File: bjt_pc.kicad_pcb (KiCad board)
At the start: 2 copper layers, 130 x 79 mm, 72 parts, among them J1 Conn_02x10_Odd_Even

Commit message: Finalized compressed 1.0
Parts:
- Qand11, Qand12, Qand13, Qand21, Qand22, Qand23, Qbuf1, Qbuf2, Qmux1, Qmux2, Qmux3, Qmux4, Qmux5, Qmux6, Qsrl1, Qsrl2, Qsrl3, Qtsb2, Qtsb3, Qtsb4, Qtsb5, Qtsb6: footprint Custom_Footprints:TO-92_Inline_disp -> Package_TO_SOT_THT:TO-92_Inline_Wide
- Qtsb1: footprint Custom_Footprints:TO-92_Inline_PNP_disp -> Package_TO_SOT_THT:TO-92_Inline_Wide
- moved R1 57.2 mm to (143.5, 105.4), turned to 90 degrees
- moved REF** 50.6 mm to (167.6, 85.0)
- moved G*** 49.4 mm to (144.0, 114.0)
- moved R4 48.9 mm to (147.3, 97.8), turned to -90 degrees
- moved Qtsb4 46.2 mm to (138.4, 94.0), turned to 0 degrees
- moved sDATA4 43.9 mm to (139.7, 105.4), turned to 90 degrees
- moved sDATA1 43.0 mm to (132.1, 92.7), turned to -90 degrees
- moved R5 42.7 mm to (154.9, 105.4), turned to 90 degrees
- moved Qmux4 40.4 mm to (130.8, 104.1), turned to 180 degrees
- moved D1 37.4 mm to (177.8, 138.4), turned to 90 degrees
- moved Qtsb2 37.0 mm to (153.7, 109.2), turned to 0 degrees
- moved C1 35.3 mm to (174.0, 88.9), turned to 90 degrees
- moved Qtsb3 34.7 mm to (146.1, 94.0), turned to 0 degrees
- moved R33 32.3 mm to (109.2, 92.7)
- moved Qmux3 32.0 mm to (123.2, 104.1), turned to 180 degrees
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- renumbered DATA to D1
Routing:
- net /DATA: track 142.5 -> 65.2 mm
- net /WE: track 105.9 -> 67.8 mm, vias 0 -> 1
- net Net-(Qsrl2-B): track 54.0 -> 16.5 mm
- net /BUSo: track 64.1 -> 28.2 mm
- net /CLK: track 107.3 -> 72.0 mm, vias 1 -> 0
- net /nOE: track 17.6 -> 38.8 mm
- net /VCC: track 326.0 -> 306.7 mm
- net /AlwaysOn: track 25.5 -> 8.67 mm
- net /BUSi: track 77.9 -> 61.2 mm, vias 0 -> 1
- net Net-(Qtsb3-C): track 34.6 -> 18.4 mm
- net /RAW: track 35.0 -> 21.1 mm
- net Net-(Qtsb5-C): track 21.0 -> 7.62 mm
- net /OE: track 16.8 -> 30.1 mm
- net /LED: track 9.65 -> 22.7 mm
- net Net-(Qmux3-C): track 37.5 -> 25.3 mm
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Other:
- board size 130 x 79 mm -> 92 x 60 mm
- board text removed: "AND2"
- board text removed: "Buffer"
- board text removed: "MUX"
- board text removed: "SR Latch"
- board text removed: "TriStateBuffer"

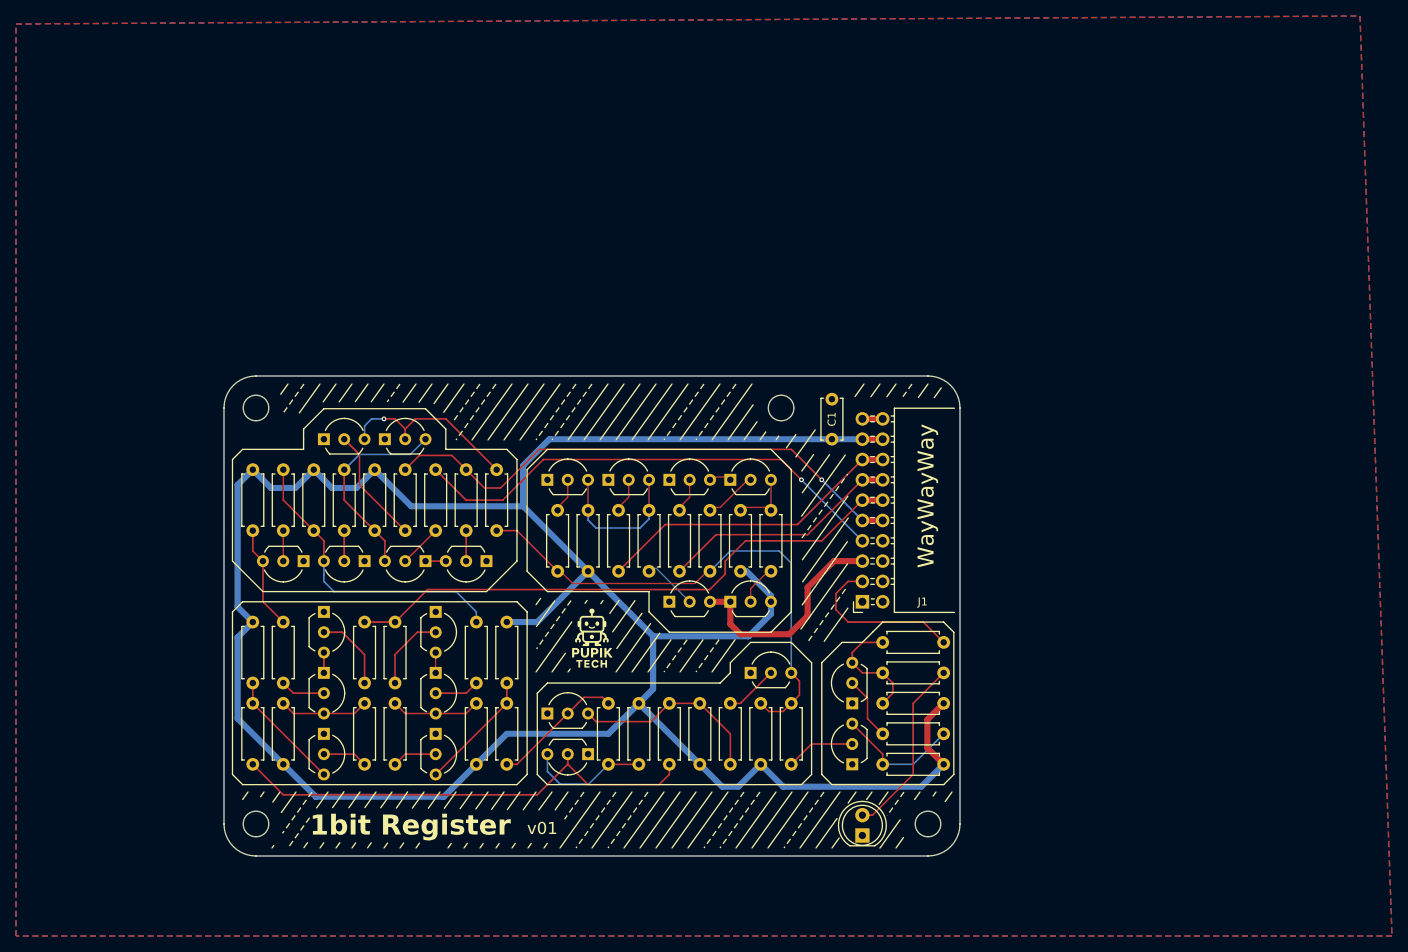
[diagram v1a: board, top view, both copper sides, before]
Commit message: Added Test Points
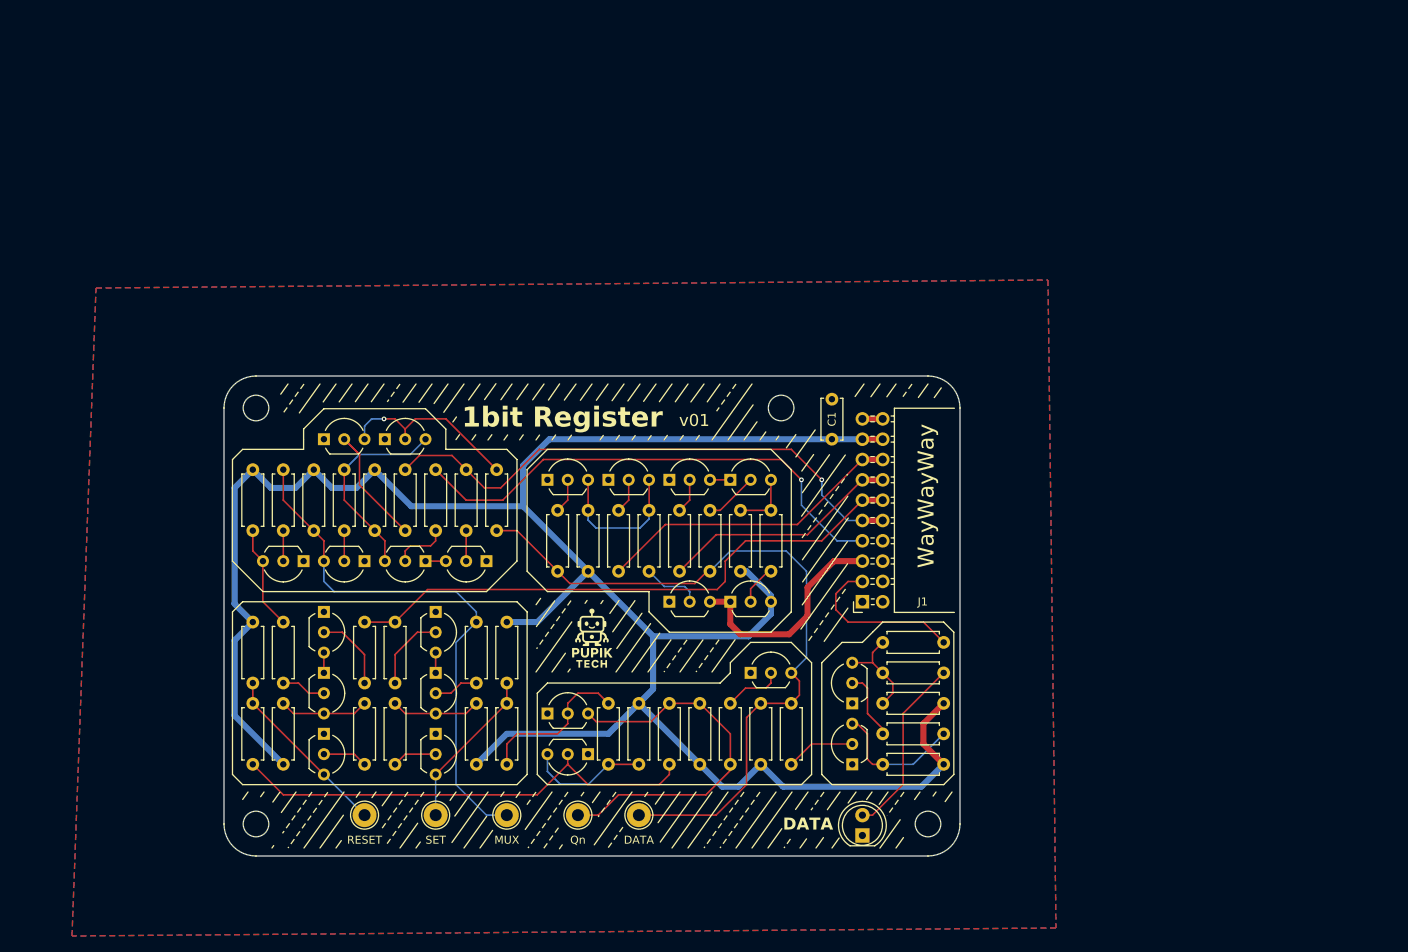
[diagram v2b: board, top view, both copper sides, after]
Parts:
- added DATA: TestPoint, TestPoint:TestPoint_THTPad_D3.0mm_Drill1.5mm, F.Cu at (149.9, 135.9)
- added MUX: TestPoint, TestPoint:TestPoint_THTPad_D3.0mm_Drill1.5mm, F.Cu at (133.3, 135.9)
- added Qn: TestPoint, TestPoint:TestPoint_THTPad_D3.0mm_Drill1.5mm, F.Cu at (142.2, 135.9)
- added RESET: TestPoint, TestPoint:TestPoint_THTPad_D3.0mm_Drill1.5mm, F.Cu at (115.6, 135.9)
- added SET: TestPoint, TestPoint:TestPoint_THTPad_D3.0mm_Drill1.5mm, F.Cu at (124.5, 135.9)
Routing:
- net Net-(Qmux2-C): track 38.0 -> 67.3 mm
- net /DATA: track 65.2 -> 92.2 mm
- net /VCC: track 306.7 -> 280.3 mm
- net Net-(Qsrl2-C): track 24.5 -> 46.7 mm
- net /R: track 15.1 -> 22.3 mm
- net /S: track 15.1 -> 20.2 mm
- net Net-(Qsrl2-B): track 16.5 -> 19.9 mm
- net Net-(Qbuf1-C): track 14.8 -> 12.3 mm
- net /BUSi: track 61.2 -> 63.1 mm
- net Net-(Qmux3-B): track 5.39 -> 6.88 mm
- net Net-(Qbuf2-C): track 15.9 -> 17.0 mm
- net /WE: track 67.8 -> 68.9 mm
- net Net-(Qsrl1-B): track 6.66 -> 7.40 mm
- net Net-(Qbuf1-B): track 7.93 -> 8.67 mm
- net Net-(Qtsb2-B): track 6.81 -> 7.40 mm
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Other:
- board text added: "DATA"

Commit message: Added back silkscreen stuff
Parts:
- renumbered C1 to C, MUX to TP1, SET to TP2, RESET to TP3, DATA to TP4, Qn to TP5
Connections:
- J1 pad 1: unconnected-(J1-Pin_1-Pad1) -> Net-(J1-Pin_1)
- J1 pad 2: unconnected-(J1-Pin_2-Pad2) -> Net-(J1-Pin_1)
- J1 pad 4: unconnected-(J1-Pin_4-Pad4) -> /RAW
- J1 pad 6: unconnected-(J1-Pin_6-Pad6) -> /BUSo
- J1 pad 8: unconnected-(J1-Pin_8-Pad8) -> /BUSi
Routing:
- net Net-(J1-Pin_1): track 0.00 -> 2.54 mm
- net /RAW: track 21.1 -> 23.7 mm
- net /BUSo: track 28.2 -> 30.8 mm
- net /BUSi: track 63.1 -> 65.6 mm
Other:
- board text added: "AND"
- board text added: "Buffer"
- board text added: "MUX"
- board text added: "Qn"
- board text added: "RESET"
- board text added: "SET"
- board text added: "SR Latch"
- board text added: "TriState Buffer"

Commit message: cleanup commit pre-purchase
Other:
- board text added: "Headers"
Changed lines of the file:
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@@
 		(tenting front back)
 		(pcbplotparams
-			(layerselection 0x00000000_00000000_55555555_f75555f5)
+			(layerselection 0x00000000_00000000_55555555_f75555ff)
 			(plot_on_all_layers_selection 0x00000000_00000000_00000000_00000000)
 			(disableapertmacros no)
-			(usegerberextensions no)
-			(usegerberattributes yes)
-			(usegerberadvancedattributes yes)
+			(usegerberextensions yes)
+			(usegerberattributes no)
+			(usegerberadvancedattributes no)
 			(creategerberjobfile yes)
 			(dashed_line_dash_ratio 12.000000)
@@
 			(pdf_back_fp_property_popups yes)
 			(pdf_metadata yes)
-			(pdf_single_document yes)
+			(pdf_single_document no)
 			(dxfpolygonmode yes)
 			(dxfimperialunits yes)
@@
 			(sketchdnponfab yes)
 			(crossoutdnponfab yes)
-			(subtractmaskfromsilk no)
-			(outputformat 4)
+			(subtractmaskfromsilk yes)
+			(outputformat 1)
 			(mirror no)
-			(drillshape 1)
+			(drillshape 0)
 			(scaleselection 1)
-			(outputdirectory "")
+			(outputdirectory "gerbers/")
 		)
 	)
@@
 		(layer "F.SilkS")
 	)
+	(gr_poly
+		(pts
+			(xy 161.4736 108.121195) (xy 166.154183 108.097204) (xy 165.663548 107.376606) (xy 165.226976 107.027182)
+			(xy 164.598373 106.736133) (xy 163.83 106.620001) (xy 162.767928 106.846817) (xy 162.14756 107.237731)
+			(xy 161.796254 107.600163)
+		)
+		(stroke
+			(width 0.15)
+			(type solid)
+		)
+		(fill yes)
+		(layer "F.SilkS")
+	)
 	(gr_line
 		(start 115 133)
@@
 		(layer "F.SilkS")
 	)
+	(gr_poly
+		(pts
+			(xy 166.154183 110.342795) (xy 161.505817 110.342795) (xy 162.03 111.069998) (xy 165.629998 111.07)
+		)
+		(stroke
+			(width 0.15)
+			(type solid)
+		)
+		(fill yes)
+		(layer "F.SilkS")
+	)
 	(gr_line
 		(start 174.890709 138.753006)
@@
 	(gr_poly
 		(pts
-			(xy 173.99 115.57) (xy 173.99 132.08) (xy 173.99 132.08) (xy 187.96 132.08) (xy 189.23 130.81) (xy 189.23 113.03)
-			(xy 187.96 111.76) (xy 180.34 111.76) (xy 179.07 113.03) (xy 177.8 114.3) (xy 175.26 114.3)
+			(xy 173.99 115.57) (xy 173.99 132.08) (xy 173.99 132.08) (xy 187.96 132.08) (xy 189.611 130.429)
+			(xy 189.611 113.411) (xy 187.96 111.76) (xy 180.34 111.76) (xy 179.07 113.03) (xy 177.8 114.3) (xy 175.26 114.3)
 		)
 		(stroke
@@
 	)
 	(gr_text "Buffer"
-		(at 184.15 122.555 90)
+		(at 184.15 122.555 270)
 		(layer "B.SilkS")
 		(effects
@@
 		)
 	)
+	(gr_text "Headers"
+		(at 186.055 97.79 270)
+		(layer "B.SilkS")
+		(effects
+			(font
+				(size 2 2)
+				(thickness 0.5)
+				(bold yes)
+			)
+			(justify mirror)
+		)
+	)
 	(gr_text "SR Latch"
-		(at 157.48 125.73 0)
+		(at 154.305 125.73 0)
 		(layer "B.SilkS")
 		(effects
@@
 	)
 	(gr_text "TriState Buffer"
-		(at 153.67 101.6 0)
+		(at 152.4 101.6 0)
 		(layer "B.SilkS")
 		(effects
